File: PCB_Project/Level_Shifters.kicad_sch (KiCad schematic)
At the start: 11 parts, among them J5 ZE27-O3, Q1 MMBT2222A, Q2 MMBT2222A, Q3 BSS138, Q4 BSS138

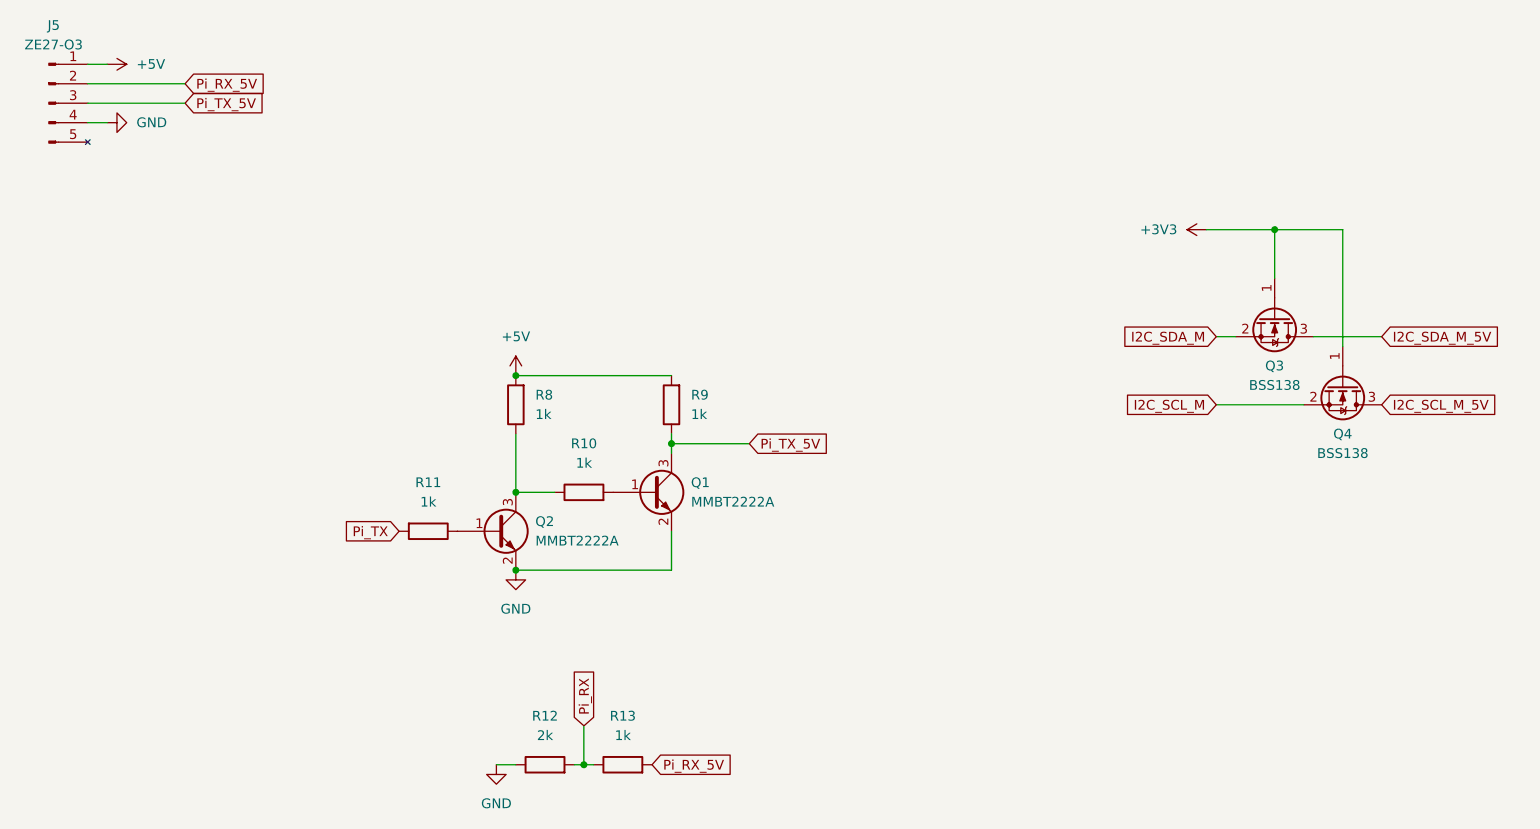
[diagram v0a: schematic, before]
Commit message: power distribution done
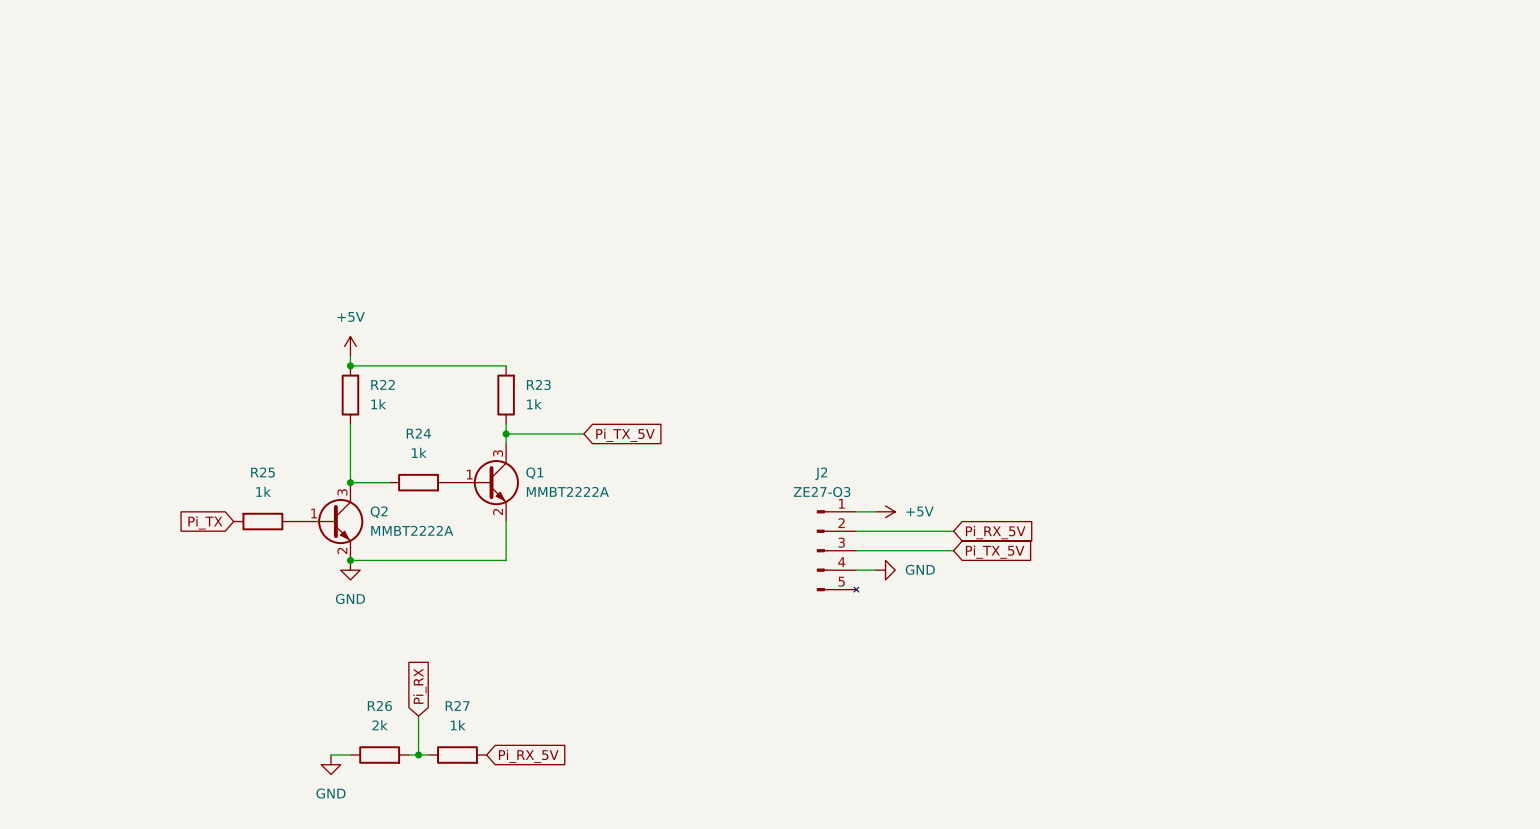
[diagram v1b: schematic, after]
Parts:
- removed Q3, Q4: BSS138, Package_TO_SOT_SMD:SOT-23, symbol Transistor_FET:BSS138
- renumbered J5 to J2, R8 to R22, R9 to R23, R10 to R24, R11 to R25, R12 to R26, R13 to R27
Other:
- moved on the sheet: J2, Q1, Q2, R22, R23, R24, R25, R26, R27

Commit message: power baby
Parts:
- renumbered J2 to J10, R22 to R15, R23 to R16, R24 to R17, R25 to R18, R26 to R19, R27 to R20
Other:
- moved on the sheet: J10
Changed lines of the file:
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@@
 	(wire
 		(pts
-			(xy 179.07 100.33) (xy 191.77 100.33)
+			(xy 187.96 100.33) (xy 200.66 100.33)
 		)
 		(stroke
@@
 	(wire
 		(pts
-			(xy 179.07 95.25) (xy 181.61 95.25)
+			(xy 187.96 95.25) (xy 190.5 95.25)
 		)
 		(stroke
@@
 	(wire
 		(pts
-			(xy 179.07 102.87) (xy 181.61 102.87)
+			(xy 187.96 102.87) (xy 190.5 102.87)
 		)
 		(stroke
@@
 	(wire
 		(pts
-			(xy 179.07 97.79) (xy 191.77 97.79)
+			(xy 187.96 97.79) (xy 200.66 97.79)
 		)
 		(stroke
@@
 	(global_label "Pi_RX_5V"
 		(shape input)
-		(at 191.77 97.79 0)
+		(at 200.66 97.79 0)
 		(fields_autoplaced yes)
 		(effects
@@
 		)
 		(property "Intersheetrefs" "${INTERSHEET_REFS}"
-			(at 203.3428 97.79 0)
+			(at 212.2328 97.79 0)
 			(effects
 				(font
@@
 	(global_label "Pi_TX_5V"
 		(shape input)
-		(at 191.77 100.33 0)
+		(at 200.66 100.33 0)
 		(fields_autoplaced yes)
 		(effects
@@
 		)
 		(property "Intersheetrefs" "${INTERSHEET_REFS}"
-			(at 203.0404 100.33 0)
+			(at 211.9304 100.33 0)
 			(effects
 				(font
@@
 		(dnp no)
 		(fields_autoplaced yes)
-		(property "Reference" "R23"
+		(property "Reference" "R16"
 			(at 135.89 78.7399 0)
 			(effects
@@
 			(project "PCB_Project"
 				(path "/3dbd20c6-0b48-4a74-89bd-dd4c54711bfb/0ea23118-6dab-4db3-8fa4-d381e9c9cbfe"
-					(reference "R23")
+					(reference "R16")
 					(unit 1)
 				)
@@
 	(symbol
 		(lib_id "power:+5V")
-		(at 181.61 95.25 270)
-		(unit 1)
-		(exclude_from_sim no)
-		(in_bom yes)
-		(on_board yes)
-		(dnp no)
-		(fields_autoplaced yes)
-		(property "Reference" "#PWR061"
-			(at 177.8 95.25 0)
+		(at 190.5 95.25 270)
+		(unit 1)
+		(exclude_from_sim no)
+		(in_bom yes)
+		(on_board yes)
+		(dnp no)
+		(fields_autoplaced yes)
+		(property "Reference" "#PWR063"
+			(at 186.69 95.25 0)
 			(effects
 				(font
@@
 		)
 		(property "Value" "+5V"
-			(at 185.42 95.2499 90)
+			(at 194.31 95.2499 90)
 			(effects
 				(font
@@
 		)
 		(property "Footprint" ""
-			(at 181.61 95.25 0)
+			(at 190.5 95.25 0)
 			(effects
 				(font
@@
 		)
 		(property "Datasheet" ""
-			(at 181.61 95.25 0)
+			(at 190.5 95.25 0)
 			(effects
 				(font
@@
 		)
 		(property "Description" "Power symbol creates a global label with name \"+5V\""
-			(at 181.61 95.25 0)
-			(effects
-				(font
-					(size 1.27 1.27)
-				)
-				(hide yes)
-			)
-		)
-		(pin "1"
-		)
-		(instances
-			(project "PCB_Project"
-				(path "/3dbd20c6-0b48-4a74-89bd-dd4c54711bfb/0ea23118-6dab-4db3-8fa4-d381e9c9cbfe"
-					(reference "#PWR061")
+			(at 190.5 95.25 0)
+			(effects
+				(font
+					(size 1.27 1.27)
+				)
+				(hide yes)
+			)
+		)
+		(pin "1"
+		)
+		(instances
+			(project "PCB_Project"
+				(path "/3dbd20c6-0b48-4a74-89bd-dd4c54711bfb/0ea23118-6dab-4db3-8fa4-d381e9c9cbfe"
+					(reference "#PWR063")
 					(unit 1)
 				)
@@
 	(symbol
 		(lib_id "power:GND")
-		(at 181.61 102.87 90)
-		(unit 1)
-		(exclude_from_sim no)
-		(in_bom yes)
-		(on_board yes)
-		(dnp no)
-		(fields_autoplaced yes)
-		(property "Reference" "#PWR062"
-			(at 187.96 102.87 0)
+		(at 190.5 102.87 90)
+		(unit 1)
+		(exclude_from_sim no)
+		(in_bom yes)
+		(on_board yes)
+		(dnp no)
+		(fields_autoplaced yes)
+		(property "Reference" "#PWR065"
+			(at 196.85 102.87 0)
 			(effects
 				(font
@@
 		)
 		(property "Value" "GND"
-			(at 185.42 102.8699 90)
+			(at 194.31 102.8699 90)
 			(effects
 				(font
@@
 		)
 		(property "Footprint" ""
-			(at 181.61 102.87 0)
+			(at 190.5 102.87 0)
 			(effects
 				(font
@@
 		)
 		(property "Datasheet" ""
-			(at 181.61 102.87 0)
+			(at 190.5 102.87 0)
 			(effects
 				(font
@@
 		)
 		(property "Description" "Power symbol creates a global label with name \"GND\" , ground"
-			(at 181.61 102.87 0)
-			(effects
-				(font
-					(size 1.27 1.27)
-				)
-				(hide yes)
-			)
-		)
-		(pin "1"
-		)
-		(instances
-			(project "PCB_Project"
-				(path "/3dbd20c6-0b48-4a74-89bd-dd4c54711bfb/0ea23118-6dab-4db3-8fa4-d381e9c9cbfe"
-					(reference "#PWR062")
+			(at 190.5 102.87 0)
+			(effects
+				(font
+					(size 1.27 1.27)
+				)
+				(hide yes)
+			)
+		)
+		(pin "1"
+		)
+		(instances
+			(project "PCB_Project"
+				(path "/3dbd20c6-0b48-4a74-89bd-dd4c54711bfb/0ea23118-6dab-4db3-8fa4-d381e9c9cbfe"
+					(reference "#PWR065")
 					(unit 1)
 				)
@@
 		(dnp no)
 		(fields_autoplaced yes)
-		(property "Reference" "R22"
+		(property "Reference" "R15"
 			(at 115.57 78.7399 0)
 			(effects
@@
 			(project "PCB_Project"
 				(path "/3dbd20c6-0b48-4a74-89bd-dd4c54711bfb/0ea23118-6dab-4db3-8fa4-d381e9c9cbfe"
-					(reference "R22")
+					(reference "R15")
 					(unit 1)
 				)
@@
 	(symbol
 		(lib_id "Connector:Conn_01x05_Pin")
-		(at 173.99 100.33 0)
-		(unit 1)
-		(exclude_from_sim no)
-		(in_bom yes)
-		(on_board yes)
-		(dnp no)
-		(fields_autoplaced yes)
-		(property "Reference" "J2"
-			(at 174.625 90.17 0)
+		(at 182.88 100.33 0)
+		(unit 1)
+		(exclude_from_sim no)
+		(in_bom yes)
+		(on_board yes)
+		(dnp no)
+		(fields_autoplaced yes)
+		(property "Reference" "J10"
+			(at 183.515 90.17 0)
 			(effects
 				(font
@@
 		)
 		(property "Value" "ZE27-O3"
-			(at 174.625 92.71 0)
+			(at 183.515 92.71 0)
 			(effects
 				(font
@@
 		)
 		(property "Footprint" "Connector_PinHeader_2.00mm:PinHeader_1x05_P2.00mm_Vertical"
-			(at 173.99 100.33 0)
+			(at 182.88 100.33 0)
 			(effects
 				(font
@@
 		)
 		(property "Datasheet" "~"
-			(at 173.99 100.33 0)
+			(at 182.88 100.33 0)
 			(effects
 				(font
@@
 		)
 		(property "Description" "ZE27-O3"
-			(at 174.244 88.646 0)
+			(at 183.134 88.646 0)
 			(effects
 				(font
@@
 			(project "PCB_Project"
 				(path "/3dbd20c6-0b48-4a74-89bd-dd4c54711bfb/0ea23118-6dab-4db3-8fa4-d381e9c9cbfe"
-					(reference "J2")
+					(reference "J10")
 					(unit 1)
 				)
@@
 		(dnp no)
 		(fields_autoplaced yes)
-		(property "Reference" "R25"
+		(property "Reference" "R18"
 			(at 101.6 90.17 90)
 			(effects
@@
 			(project "PCB_Project"
 				(path "/3dbd20c6-0b48-4a74-89bd-dd4c54711bfb/0ea23118-6dab-4db3-8fa4-d381e9c9cbfe"
-					(reference "R25")
+					(reference "R18")
 					(unit 1)
 				)
@@
 		(dnp no)
 		(fields_autoplaced yes)
-		(property "Reference" "R27"
+		(property "Reference" "R20"
 			(at 127 120.65 90)
 			(effects
@@
 			(project "PCB_Project"
 				(path "/3dbd20c6-0b48-4a74-89bd-dd4c54711bfb/0ea23118-6dab-4db3-8fa4-d381e9c9cbfe"
-					(reference "R27")
+					(reference "R20")
 					(unit 1)
 				)
@@
 		(dnp no)
 		(fields_autoplaced yes)
-		(property "Reference" "#PWR065"
+		(property "Reference" "#PWR064"
 			(at 113.03 107.95 0)
 			(effects
@@
 			(project "PCB_Project"
 				(path "/3dbd20c6-0b48-4a74-89bd-dd4c54711bfb/0ea23118-6dab-4db3-8fa4-d381e9c9cbfe"
-					(reference "#PWR065")
+					(reference "#PWR064")
 					(unit 1)
 				)
@@
 		(dnp no)
 		(fields_autoplaced yes)
-		(property "Reference" "R26"
+		(property "Reference" "R19"
 			(at 116.84 120.65 90)
 			(effects
@@
 			(project "PCB_Project"
 				(path "/3dbd20c6-0b48-4a74-89bd-dd4c54711bfb/0ea23118-6dab-4db3-8fa4-d381e9c9cbfe"
-					(reference "R26")
+					(reference "R19")
 					(unit 1)
 				)
@@
 		(dnp no)
 		(fields_autoplaced yes)
-		(property "Reference" "R24"
+		(property "Reference" "R17"
 			(at 121.92 85.09 90)
 			(effects
@@
 			(project "PCB_Project"
 				(path "/3dbd20c6-0b48-4a74-89bd-dd4c54711bfb/0ea23118-6dab-4db3-8fa4-d381e9c9cbfe"
-					(reference "R24")
+					(reference "R17")
 					(unit 1)
 				)
@@
 		(dnp no)
 		(fields_autoplaced yes)
-		(property "Reference" "#PWR063"
+		(property "Reference" "#PWR062"
 			(at 113.03 78.74 0)
 			(effects
@@
 			(project "PCB_Project"
 				(path "/3dbd20c6-0b48-4a74-89bd-dd4c54711bfb/0ea23118-6dab-4db3-8fa4-d381e9c9cbfe"
-					(reference "#PWR063")
-					(unit 1)
-				)
+					(reference "#PWR062")
+					(unit 1)
+				)

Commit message: working on pcb
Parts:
- renumbered J10 to J11, R15 to R20, R16 to R21, R17 to R22, R18 to R23, R19 to R24, R20 to R25
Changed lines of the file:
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@@
 		(dnp no)
 		(fields_autoplaced yes)
-		(property "Reference" "R16"
+		(property "Reference" "R21"
 			(at 135.89 78.7399 0)
 			(effects
@@
 			(project "PCB_Project"
 				(path "/3dbd20c6-0b48-4a74-89bd-dd4c54711bfb/0ea23118-6dab-4db3-8fa4-d381e9c9cbfe"
-					(reference "R16")
+					(reference "R21")
 					(unit 1)
 				)
@@
 		(dnp no)
 		(fields_autoplaced yes)
-		(property "Reference" "#PWR063"
+		(property "Reference" "#PWR085"
 			(at 186.69 95.25 0)
 			(effects
@@
 			(project "PCB_Project"
 				(path "/3dbd20c6-0b48-4a74-89bd-dd4c54711bfb/0ea23118-6dab-4db3-8fa4-d381e9c9cbfe"
-					(reference "#PWR063")
+					(reference "#PWR085")
 					(unit 1)
 				)
@@
 		(dnp no)
 		(fields_autoplaced yes)
-		(property "Reference" "#PWR065"
+		(property "Reference" "#PWR087"
 			(at 196.85 102.87 0)
 			(effects
@@
 			(project "PCB_Project"
 				(path "/3dbd20c6-0b48-4a74-89bd-dd4c54711bfb/0ea23118-6dab-4db3-8fa4-d381e9c9cbfe"
-					(reference "#PWR065")
+					(reference "#PWR087")
 					(unit 1)
 				)
@@
 		(dnp no)
 		(fields_autoplaced yes)
-		(property "Reference" "R15"
+		(property "Reference" "R20"
 			(at 115.57 78.7399 0)
 			(effects
@@
 			(project "PCB_Project"
 				(path "/3dbd20c6-0b48-4a74-89bd-dd4c54711bfb/0ea23118-6dab-4db3-8fa4-d381e9c9cbfe"
-					(reference "R15")
+					(reference "R20")
 					(unit 1)
 				)
@@
 		(dnp no)
 		(fields_autoplaced yes)
-		(property "Reference" "#PWR066"
+		(property "Reference" "#PWR088"
 			(at 110.49 133.35 0)
 			(effects
@@
 			(project "PCB_Project"
 				(path "/3dbd20c6-0b48-4a74-89bd-dd4c54711bfb/0ea23118-6dab-4db3-8fa4-d381e9c9cbfe"
-					(reference "#PWR066")
+					(reference "#PWR088")
 					(unit 1)
 				)
@@
 		(dnp no)
 		(fields_autoplaced yes)
-		(property "Reference" "J10"
+		(property "Reference" "J11"
 			(at 183.515 90.17 0)
 			(effects
@@
 			(project "PCB_Project"
 				(path "/3dbd20c6-0b48-4a74-89bd-dd4c54711bfb/0ea23118-6dab-4db3-8fa4-d381e9c9cbfe"
-					(reference "J10")
+					(reference "J11")
 					(unit 1)
 				)
@@
 		(dnp no)
 		(fields_autoplaced yes)
-		(property "Reference" "R18"
+		(property "Reference" "R23"
 			(at 101.6 90.17 90)
 			(effects
@@
 			(project "PCB_Project"
 				(path "/3dbd20c6-0b48-4a74-89bd-dd4c54711bfb/0ea23118-6dab-4db3-8fa4-d381e9c9cbfe"
-					(reference "R18")
+					(reference "R23")
 					(unit 1)
 				)
@@
 		(dnp no)
 		(fields_autoplaced yes)
-		(property "Reference" "R20"
+		(property "Reference" "R25"
 			(at 127 120.65 90)
 			(effects
@@
 			(project "PCB_Project"
 				(path "/3dbd20c6-0b48-4a74-89bd-dd4c54711bfb/0ea23118-6dab-4db3-8fa4-d381e9c9cbfe"
-					(reference "R20")
+					(reference "R25")
 					(unit 1)
 				)
@@
 		(dnp no)
 		(fields_autoplaced yes)
-		(property "Reference" "#PWR064"
+		(property "Reference" "#PWR086"
 			(at 113.03 107.95 0)
 			(effects
@@
 			(project "PCB_Project"
 				(path "/3dbd20c6-0b48-4a74-89bd-dd4c54711bfb/0ea23118-6dab-4db3-8fa4-d381e9c9cbfe"
-					(reference "#PWR064")
+					(reference "#PWR086")
 					(unit 1)
 				)
@@
 		(dnp no)
 		(fields_autoplaced yes)
-		(property "Reference" "R19"
+		(property "Reference" "R24"
 			(at 116.84 120.65 90)
 			(effects
@@
 			(project "PCB_Project"
 				(path "/3dbd20c6-0b48-4a74-89bd-dd4c54711bfb/0ea23118-6dab-4db3-8fa4-d381e9c9cbfe"
-					(reference "R19")
+					(reference "R24")
 					(unit 1)
 				)
@@
 		(dnp no)
 		(fields_autoplaced yes)
-		(property "Reference" "R17"
+		(property "Reference" "R22"
 			(at 121.92 85.09 90)
 			(effects
@@
 			(project "PCB_Project"
 				(path "/3dbd20c6-0b48-4a74-89bd-dd4c54711bfb/0ea23118-6dab-4db3-8fa4-d381e9c9cbfe"
-					(reference "R17")
+					(reference "R22")
 					(unit 1)
 				)
@@
 		(dnp no)
 		(fields_autoplaced yes)
-		(property "Reference" "#PWR062"
+		(property "Reference" "#PWR084"
 			(at 113.03 78.74 0)
 			(effects
@@
 			(project "PCB_Project"
 				(path "/3dbd20c6-0b48-4a74-89bd-dd4c54711bfb/0ea23118-6dab-4db3-8fa4-d381e9c9cbfe"
-					(reference "#PWR062")
-					(unit 1)
-				)
+					(reference "#PWR084")
+					(unit 1)
+				)

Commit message: finally
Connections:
- net +5V renamed +5.25V
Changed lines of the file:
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@@
+	)
+	(symbol
+		(lib_id "power:+5V")
+		(at 190.5 95.25 270)
+		(unit 1)
+		(exclude_from_sim no)
+		(in_bom yes)
+		(on_board yes)
+		(dnp no)
+		(fields_autoplaced yes)
+		(property "Reference" "#PWR03"
+			(at 186.69 95.25 0)
+			(effects
+				(font
+					(size 1.27 1.27)
+				)
+				(hide yes)
+			)
+		)
+		(property "Value" "+5.25V"
+			(at 194.31 95.2499 90)
+			(effects
+				(font
+					(size 1.27 1.27)
+				)
+				(justify left)
+			)
+		)
+		(property "Footprint" ""
+			(at 190.5 95.25 0)
+			(effects
+				(font
+					(size 1.27 1.27)
+				)
+				(hide yes)
+			)
+		)
+		(property "Datasheet" ""
+			(at 190.5 95.25 0)
+			(effects
+				(font
+					(size 1.27 1.27)
+				)
+				(hide yes)
+			)
+		)
+		(property "Description" "Power symbol creates a global label with name \"+5V\""
+			(at 190.5 95.25 0)
+			(effects
+				(font
+					(size 1.27 1.27)
+				)
+				(hide yes)
+			)
+		)
+		(pin "1"
+		)
+		(instances
+			(project "PCB_Project"
+				(path "/3dbd20c6-0b48-4a74-89bd-dd4c54711bfb/0ea23118-6dab-4db3-8fa4-d381e9c9cbfe"
+					(reference "#PWR03")
+					(unit 1)
+				)
+			)
+		)
 	)
 	(symbol
@@
 	)
 	(symbol
-		(lib_id "power:+5V")
-		(at 190.5 95.25 270)
-		(unit 1)
-		(exclude_from_sim no)
-		(in_bom yes)
-		(on_board yes)
-		(dnp no)
-		(fields_autoplaced yes)
-		(property "Reference" "#PWR085"
-			(at 186.69 95.25 0)
-			(effects
-				(font
-					(size 1.27 1.27)
-				)
-				(hide yes)
-			)
-		)
-		(property "Value" "+5V"
-			(at 194.31 95.2499 90)
-			(effects
-				(font
-					(size 1.27 1.27)
-				)
-				(justify left)
-			)
-		)
-		(property "Footprint" ""
-			(at 190.5 95.25 0)
-			(effects
-				(font
-					(size 1.27 1.27)
-				)
-				(hide yes)
-			)
-		)
-		(property "Datasheet" ""
-			(at 190.5 95.25 0)
-			(effects
-				(font
-					(size 1.27 1.27)
-				)
-				(hide yes)
-			)
-		)
-		(property "Description" "Power symbol creates a global label with name \"+5V\""
-			(at 190.5 95.25 0)
-			(effects
-				(font
-					(size 1.27 1.27)
-				)
-				(hide yes)
-			)
-		)
-		(pin "1"
-		)
-		(instances
-			(project "PCB_Project"
-				(path "/3dbd20c6-0b48-4a74-89bd-dd4c54711bfb/0ea23118-6dab-4db3-8fa4-d381e9c9cbfe"
-					(reference "#PWR085")
-					(unit 1)
-				)
-			)
-		)
-	)
-	(symbol
 		(lib_id "power:GND")
 		(at 190.5 102.87 90)
@@
 	)
 	(symbol
+		(lib_id "power:+5V")
+		(at 113.03 74.93 0)
+		(unit 1)
+		(exclude_from_sim no)
+		(in_bom yes)
+		(on_board yes)
+		(dnp no)
+		(fields_autoplaced yes)
+		(property "Reference" "#PWR074"
+			(at 113.03 78.74 0)
+			(effects
+				(font
+					(size 1.27 1.27)
+				)
+				(hide yes)
+			)
+		)
+		(property "Value" "+5.25V"
+			(at 113.03 69.85 0)
+			(effects
+				(font
+					(size 1.27 1.27)
+				)
+			)
+		)
+		(property "Footprint" ""
+			(at 113.03 74.93 0)
+			(effects
+				(font
+					(size 1.27 1.27)
+				)
+				(hide yes)
+			)
+		)
+		(property "Datasheet" ""
+			(at 113.03 74.93 0)
+			(effects
+				(font
+					(size 1.27 1.27)
+				)
+				(hide yes)
+			)
+		)
+		(property "Description" "Power symbol creates a global label with name \"+5V\""
+			(at 113.03 74.93 0)
+			(effects
+				(font
+					(size 1.27 1.27)
+				)
+				(hide yes)
+			)
+		)
+		(pin "1"
+		)
+		(instances
+			(project "PCB_Project"
+				(path "/3dbd20c6-0b48-4a74-89bd-dd4c54711bfb/0ea23118-6dab-4db3-8fa4-d381e9c9cbfe"
+					(reference "#PWR074")
+					(unit 1)
+				)
+			)
+		)
+	)
+	(symbol
 		(lib_id "power:GND")
 		(at 113.03 101.6 0)
@@
 					(unit 1)
 				)
-			)
-		)
-	)
-	(symbol
-		(lib_id "power:+5V")
-		(at 113.03 74.93 0)
-		(unit 1)
-		(exclude_from_sim no)
-		(in_bom yes)
-		(on_board yes)
-		(dnp no)
-		(fields_autoplaced yes)
-		(property "Reference" "#PWR084"
-			(at 113.03 78.74 0)
-			(effects
-				(font
-					(size 1.27 1.27)
-				)
-				(hide yes)
-			)
-		)
-		(property "Value" "+5V"
-			(at 113.03 69.85 0)
-			(effects
-				(font
-					(size 1.27 1.27)
-				)
-			)
-		)
-		(property "Footprint" ""
-			(at 113.03 74.93 0)
-			(effects
-				(font
-					(size 1.27 1.27)
-				)
-				(hide yes)
-			)
-		)
-		(property "Datasheet" ""
-			(at 113.03 74.93 0)
-			(effects
-				(font
-					(size 1.27 1.27)
-				)
-				(hide yes)
-			)
-		)
-		(property "Description" "Power symbol creates a global label with name \"+5V\""
-			(at 113.03 74.93 0)
-			(effects
-				(font
-					(size 1.27 1.27)
-				)
-				(hide yes)
-			)
-		)
-		(pin "1"
-		)
-		(instances
-			(project "PCB_Project"
-				(path "/3dbd20c6-0b48-4a74-89bd-dd4c54711bfb/0ea23118-6dab-4db3-8fa4-d381e9c9cbfe"
-					(reference "#PWR084")
-					(unit 1)
-				)
